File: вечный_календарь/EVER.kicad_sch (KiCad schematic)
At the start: 44 parts, among them U1 YAAJ_DCDC_StepUp_SX1308, U2 ESP32-H2-DEVKITM-1-N4

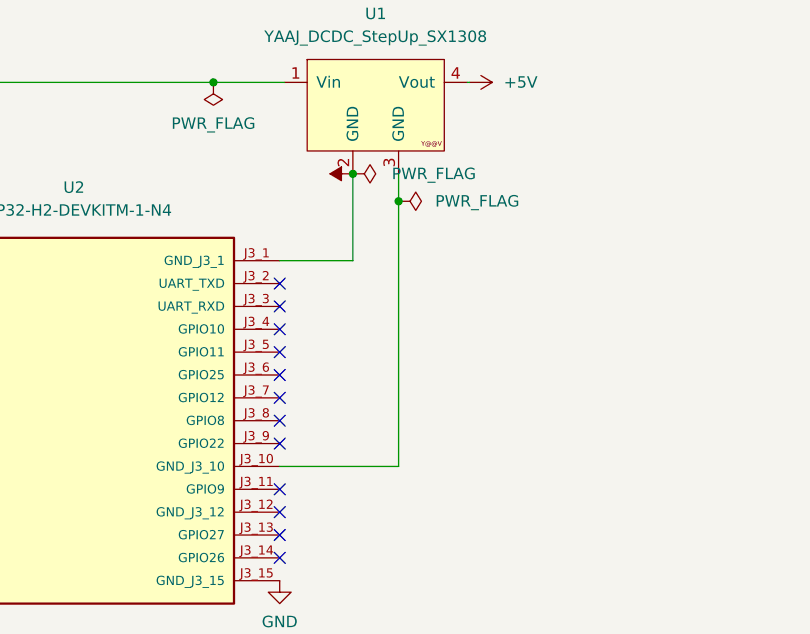
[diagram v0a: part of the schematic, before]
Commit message: endless_calendar: минорное изменение
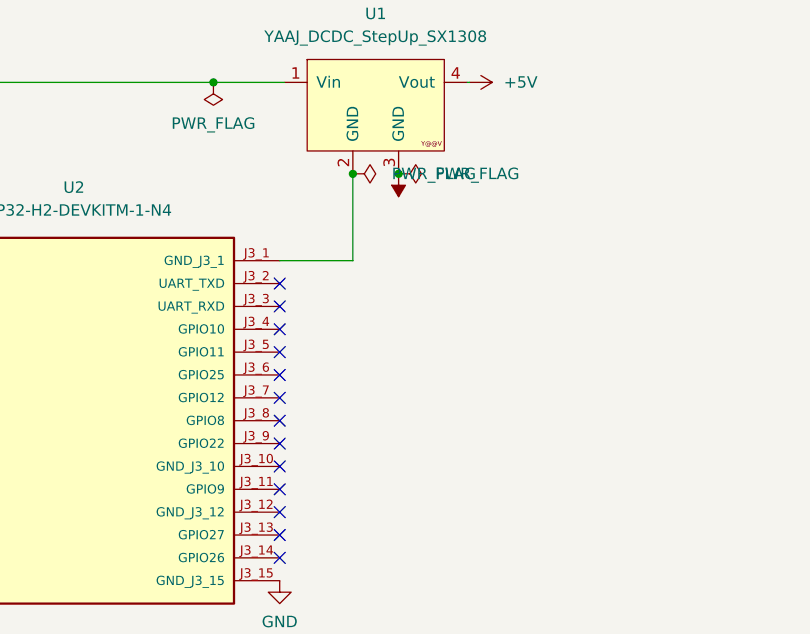
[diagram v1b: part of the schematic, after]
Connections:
- net -BATT: now also U1.3 (GND); no longer U1.2 (GND), U2.J3_1 (GND_J3_1)
- net at U2.J3_10 (GND_J3_10): no longer U1.3 (GND)
- new net: U1.2 (GND), U2.J3_1 (GND_J3_1)
- no-connect marks 25 -> 26
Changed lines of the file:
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@@
 	(paper "A2")
 	(junction
-		(at 429.26 277.622)
+		(at 408.686 264.414)
 		(diameter 0)
 		(color 0 0 0 0)
 	)
 	(junction
-		(at 408.686 264.414)
+		(at 429.26 274.574)
 		(diameter 0)
 		(color 0 0 0 0)
@@
 	)
 	(no_connect
+		(at 416.052 307.086)
+	)
+	(no_connect
 		(at 416.052 304.546)
 	)
@@
 	(wire
 		(pts
-			(xy 429.26 277.622) (xy 429.26 274.574)
-		)
-		(stroke
-			(width 0)
-			(type default)
-		)
-	)
-	(wire
-		(pts
 			(xy 468.884 150.114) (xy 474.726 150.114)
 		)
@@
 		)
 	)
-	(wire
-		(pts
-			(xy 416.052 307.086) (xy 429.26 307.086)
-		)
-		(stroke
-			(width 0)
-			(type default)
-		)
-	)
-	(wire
-		(pts
-			(xy 429.26 307.086) (xy 429.26 277.622)
-		)
-		(stroke
-			(width 0)
-			(type default)
-		)
-	)
 	(label "DATA"
 		(at 370.332 302.006 180)
@@
 	)
 	(symbol
-		(lib_id "power:-BATT")
-		(at 424.18 274.574 90)
-		(unit 1)
-		(exclude_from_sim no)
-		(in_bom yes)
-		(on_board yes)
-		(dnp no)
-		(fields_autoplaced yes)
-		(property "Reference" "#PWR087"
-			(at 427.99 274.574 0)
-			(effects
-				(font
-					(size 1.27 1.27)
-				)
-				(hide yes)
-			)
-		)
-		(property "Value" "-BATT"
-			(at 420.624 274.5739 90)
-			(effects
-				(font
-					(size 1.27 1.27)
-				)
-				(justify left)
-				(hide yes)
-			)
-		)
-		(property "Footprint" ""
-			(at 424.18 274.574 0)
-			(effects
-				(font
-					(size 1.27 1.27)
-				)
-				(hide yes)
-			)
-		)
-		(property "Datasheet" ""
-			(at 424.18 274.574 0)
-			(effects
-				(font
-					(size 1.27 1.27)
-				)
-				(hide yes)
-			)
-		)
-		(property "Description" "Power symbol creates a global label with name \"-BATT\""
-			(at 424.18 274.574 0)
-			(effects
-				(font
-					(size 1.27 1.27)
-				)
-				(hide yes)
-			)
-		)
-		(pin "1"
-		)
-		(instances
-			(project "EVER"
-				(path "/c992b362-f2b9-4217-ac9e-39c44f1b4796"
-					(reference "#PWR087")
-					(unit 1)
-				)
-			)
-		)
-	)
-	(symbol
 		(lib_id "LED:WS2812B")
 		(at 446.278 68.834 0)
@@
 	)
 	(symbol
+		(lib_id "power:-BATT")
+		(at 429.26 274.574 180)
+		(unit 1)
+		(exclude_from_sim no)
+		(in_bom yes)
+		(on_board yes)
+		(dnp no)
+		(fields_autoplaced yes)
+		(property "Reference" "#PWR085"
+			(at 429.26 270.764 0)
+			(effects
+				(font
+					(size 1.27 1.27)
+				)
+				(hide yes)
+			)
+		)
+		(property "Value" "-BATT"
+			(at 429.2599 278.13 90)
+			(effects
+				(font
+					(size 1.27 1.27)
+				)
+				(justify left)
+				(hide yes)
+			)
+		)
+		(property "Footprint" ""
+			(at 429.26 274.574 0)
+			(effects
+				(font
+					(size 1.27 1.27)
+				)
+				(hide yes)
+			)
+		)
+		(property "Datasheet" ""
+			(at 429.26 274.574 0)
+			(effects
+				(font
+					(size 1.27 1.27)
+				)
+				(hide yes)
+			)
+		)
+		(property "Description" "Power symbol creates a global label with name \"-BATT\""
+			(at 429.26 274.574 0)
+			(effects
+				(font
+					(size 1.27 1.27)
+				)
+				(hide yes)
+			)
+		)
+		(pin "1"
+		)
+		(instances
+			(project "EVER"
+				(path "/c992b362-f2b9-4217-ac9e-39c44f1b4796"
+					(reference "#PWR085")
+					(unit 1)
+				)
+			)
+		)
+	)
+	(symbol
 		(lib_id "LED:WS2812B")
 		(at 430.784 122.174 0)
@@
 	(symbol
 		(lib_id "power:PWR_FLAG")
-		(at 429.26 277.622 270)
+		(at 429.26 274.574 270)
 		(unit 1)
 		(exclude_from_sim no)
@@
 		(fields_autoplaced yes)
 		(property "Reference" "#FLG04"
-			(at 431.165 277.622 0)
+			(at 431.165 274.574 0)
 			(effects
 				(font
@@
 		)
 		(property "Value" "PWR_FLAG"
-			(at 433.324 277.6219 90)
+			(at 433.324 274.5739 90)
 			(effects
 				(font
@@
 		)
 		(property "Footprint" ""
-			(at 429.26 277.622 0)
+			(at 429.26 274.574 0)
 			(effects
 				(font
@@
 		)
 		(property "Datasheet" "~"
-			(at 429.26 277.622 0)
+			(at 429.26 274.574 0)
 			(effects
 				(font
@@
 		)
 		(property "Description" "Special symbol for telling ERC where power comes from"
-			(at 429.26 277.622 0)
+			(at 429.26 274.574 0)
 			(effects
 				(font

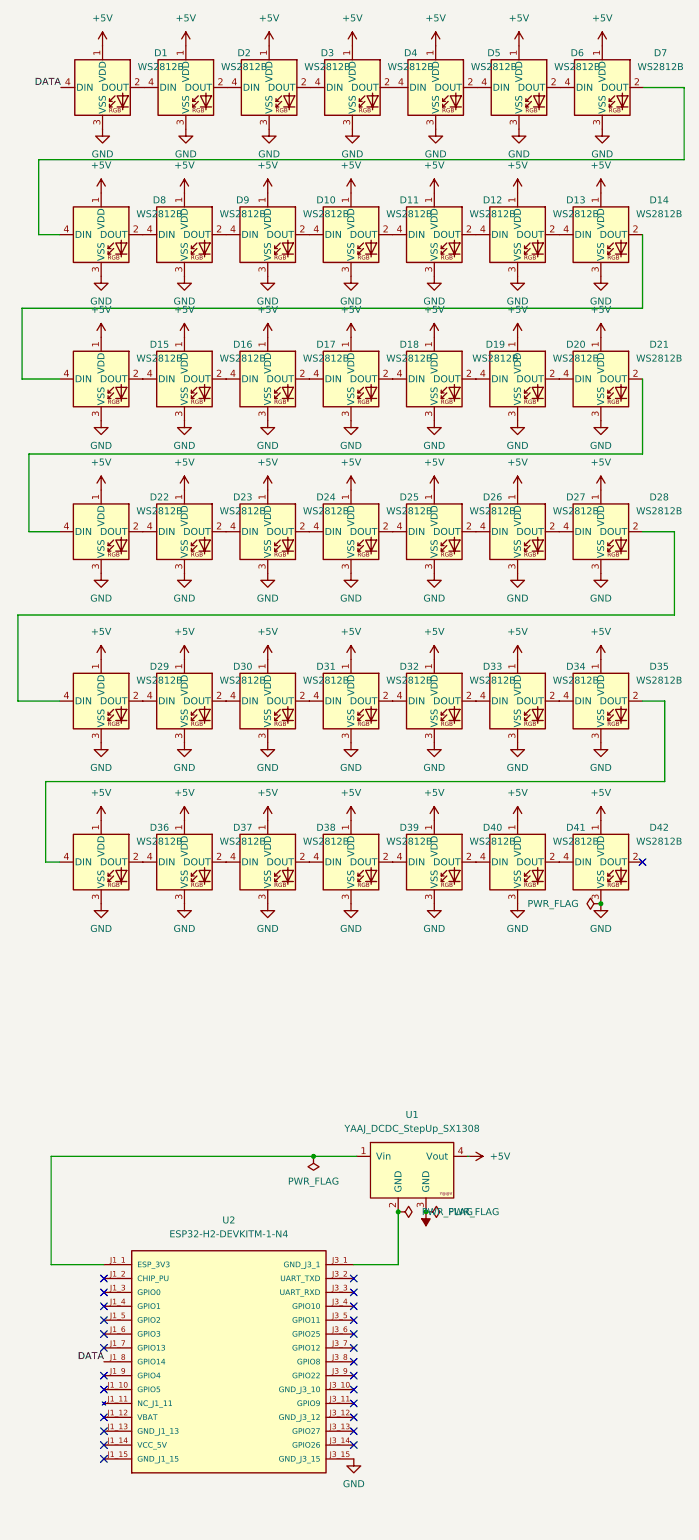
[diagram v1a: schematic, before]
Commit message: endless_calendar: h2 -> s3 devkit; resistors added; added example for arduino code
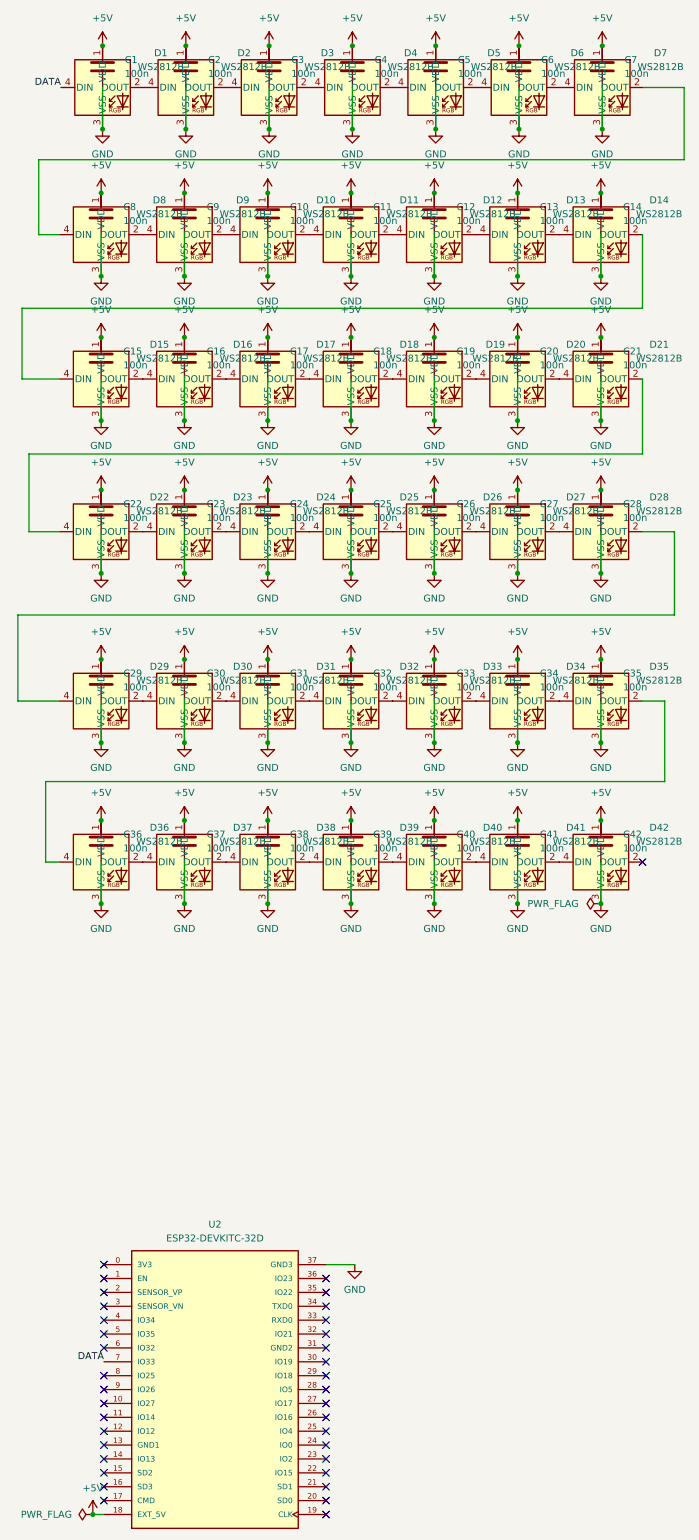
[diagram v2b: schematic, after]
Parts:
- removed U1: YAAJ_DCDC_StepUp_SX1308, dcdc_stepup_sx1308:YAAJ_DCDC_StepUp_SX1308, symbol dcdc_stepup_sx1308:YAAJ_DCDC_StepUp_SX1308
- removed U2: ESP32-H2-DEVKITM-1-N4, ESP32-H2-DEVKITM-1-N4:MODULE_ESP32-H2-DEVKITM-1-N4, symbol ESP32-H2-DEVKITM-1-N4:ESP32-H2-DEVKITM-1-N4
- added C1, C10, C11, C12, C13, C14, C15, C16, C17, C18, C19, C2, C20, C21, C22, C23, C24, C25, C26, C27, C28, C29, C3, C30, C31, C32, C33, C34, C35, C36, C37, C38, C39, C4, C40, C41, C42, C5, C6, C7, C8, C9: 100n, Capacitor_SMD:C_0805_2012Metric_Pad1.18x1.45mm_HandSolder, symbol Device:C
- added U2: ESP32-DEVKITC-32D, ESP32-DEVKITC-32D:MODULE_ESP32-DEVKITC-32D, symbol ESP32-DEVKITC-32D:ESP32-DEVKITC-32D
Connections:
- net +5V: now also C1.1, C10.1, C11.1, C12.1, C13.1, C14.1, C15.1, C16.1, C17.1, C18.1, C19.1, C2.1, C20.1, C21.1, C22.1, C23.1, C24.1, C25.1, C26.1, C27.1, C28.1, C29.1, C3.1, C30.1, C31.1, C32.1, C33.1, C34.1, C35.1, C36.1, C37.1, C38.1, C39.1, C4.1, C40.1, C41.1, C42.1, C5.1, C6.1, C7.1, C8.1, C9.1, U2.18 (EXT_5V)
- net DATA: now also U2.7 (IO33)
- net GND: now also C1.2, C10.2, C11.2, C12.2, C13.2, C14.2, C15.2, C16.2, C17.2, C18.2, C19.2, C2.2, C20.2, C21.2, C22.2, C23.2, C24.2, C25.2, C26.2, C27.2, C28.2, C29.2, C3.2, C30.2, C31.2, C32.2, C33.2, C34.2, C35.2, C36.2, C37.2, C38.2, C39.2, C4.2, C40.2, C41.2, C42.2, C5.2, C6.2, C7.2, C8.2, C9.2, U2.37 (GND3)
- no-connect marks 26 -> 36
